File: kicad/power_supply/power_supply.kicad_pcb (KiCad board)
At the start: 2 copper layers, 36.6 x 24.1 mm, 18 parts, among them J1 USB_C_Receptacle_PowerOnly_6P, J2 Battery terminal, J3 Base board terminal, Q1 DMG2301L, U1 MCP1640x-xCHY, U2 MCP73831-2-OT

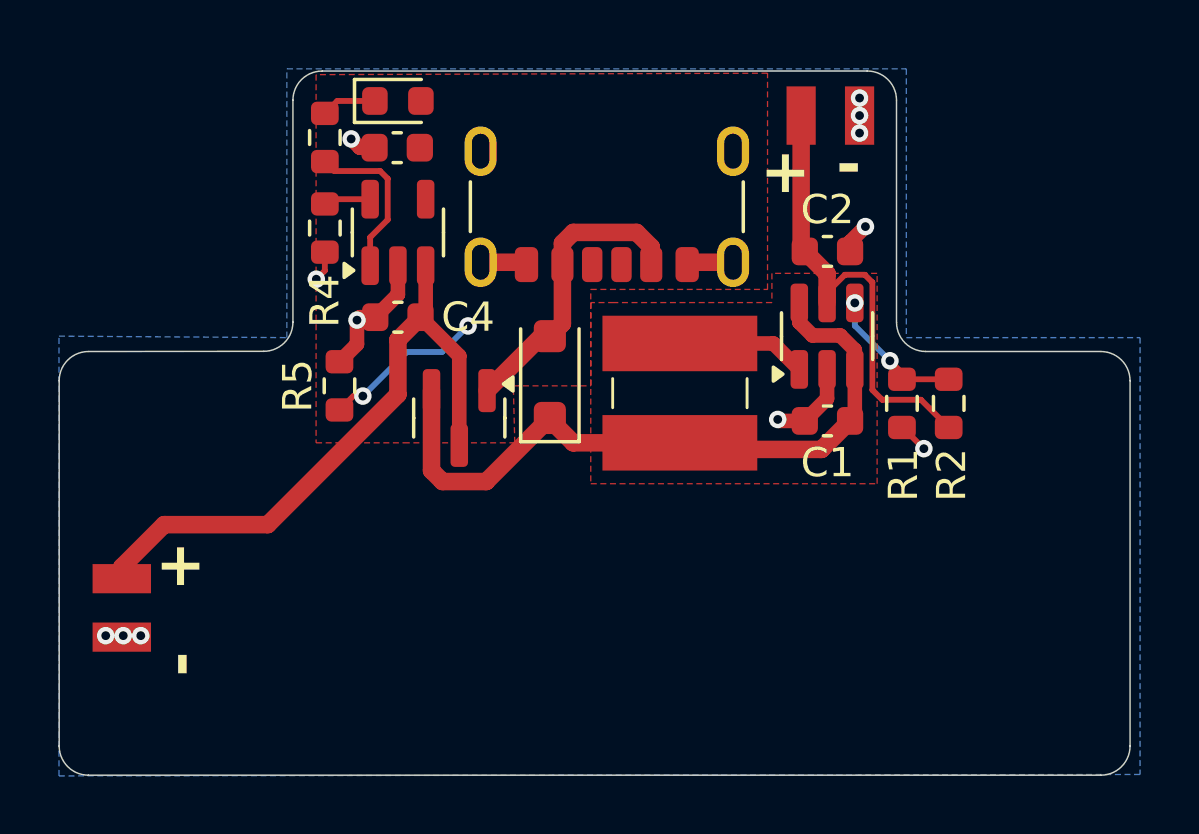
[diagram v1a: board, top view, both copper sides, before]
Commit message: pcbs: improve powering scheme, redesign cartridge; 3dcad: update whole housing
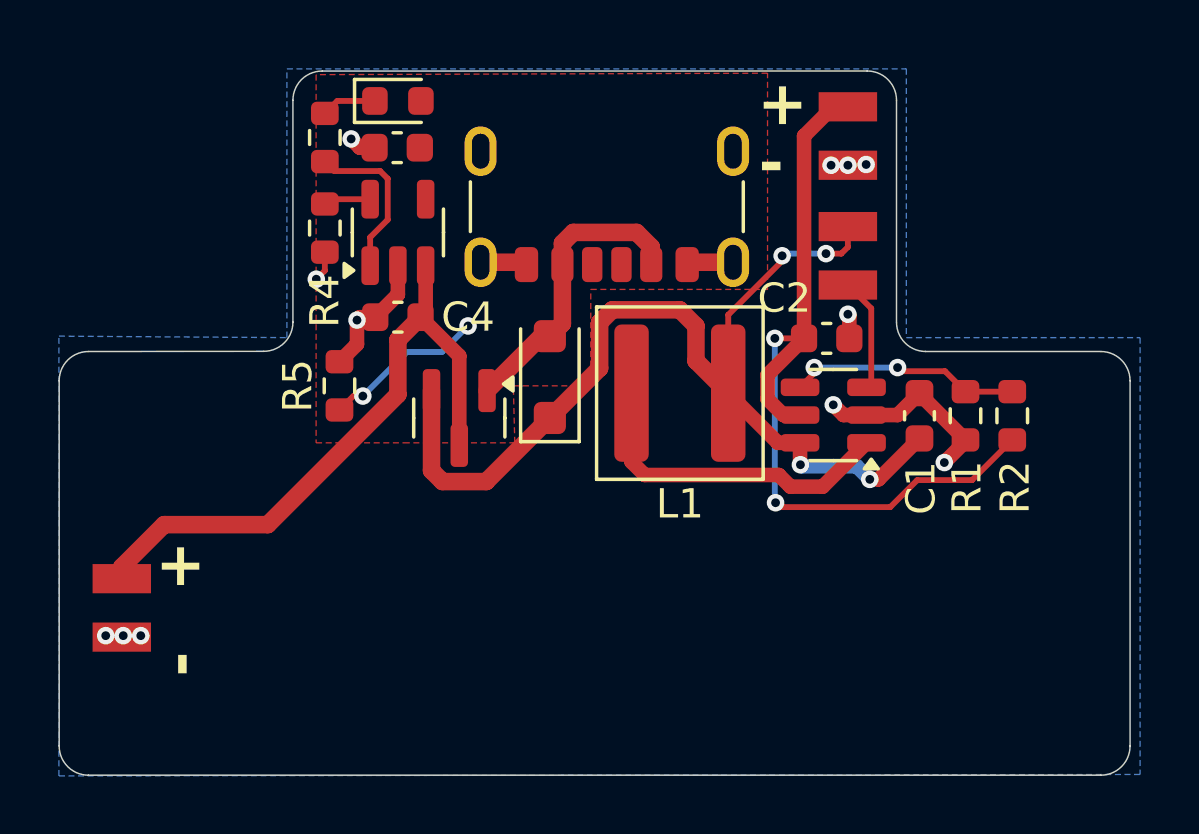
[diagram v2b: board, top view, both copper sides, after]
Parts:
- added J4: Short if cartridge present, components:Pads_1x2mm_2x, F.Cu at (152.0, 82.2)
- J3: value Base board terminal -> Base board power terminal
- L1: footprint components:CDRH4D18 -> Inductor_SMD:L_Coilcraft_XAL5050-XXX
- moved C1 3.15 mm to (154.4, 87.7), turned to 90 degrees
- moved C2 2.98 mm to (151.3, 85.0)
- moved U1 2.71 mm to (151.5, 87.7), turned to 180 degrees
- moved R1 2.22 mm to (156.0, 87.7)
- moved R2 2.22 mm to (157.6, 87.7)
- moved J3 0.92 mm to (152.0, 78.1), turned to -90 degrees
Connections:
- U1 pad 3: VSYS -> Net-(J4-Pin_1)
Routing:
- net Net-(J3-Pin_1): track 16.3 -> 28.5 mm, vias 0 -> 2
- net VSYS: track 24.4 -> 35.7 mm, vias 0 -> 4
- net Net-(U1-SW): track 4.46 -> 11.4 mm
- net Net-(J4-Pin_1): track 0.00 -> 3.90 mm
- net Net-(U1-V_{FB}): track 4.88 -> 7.99 mm
- net GND: track 14.7 -> 17.2 mm
- removed copper zone on F.Cu, net VSYS

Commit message: 3dcad/housing: fdm & sla variants; kicad/power_supply: add p-down resistor to the MCP1640's EN pin
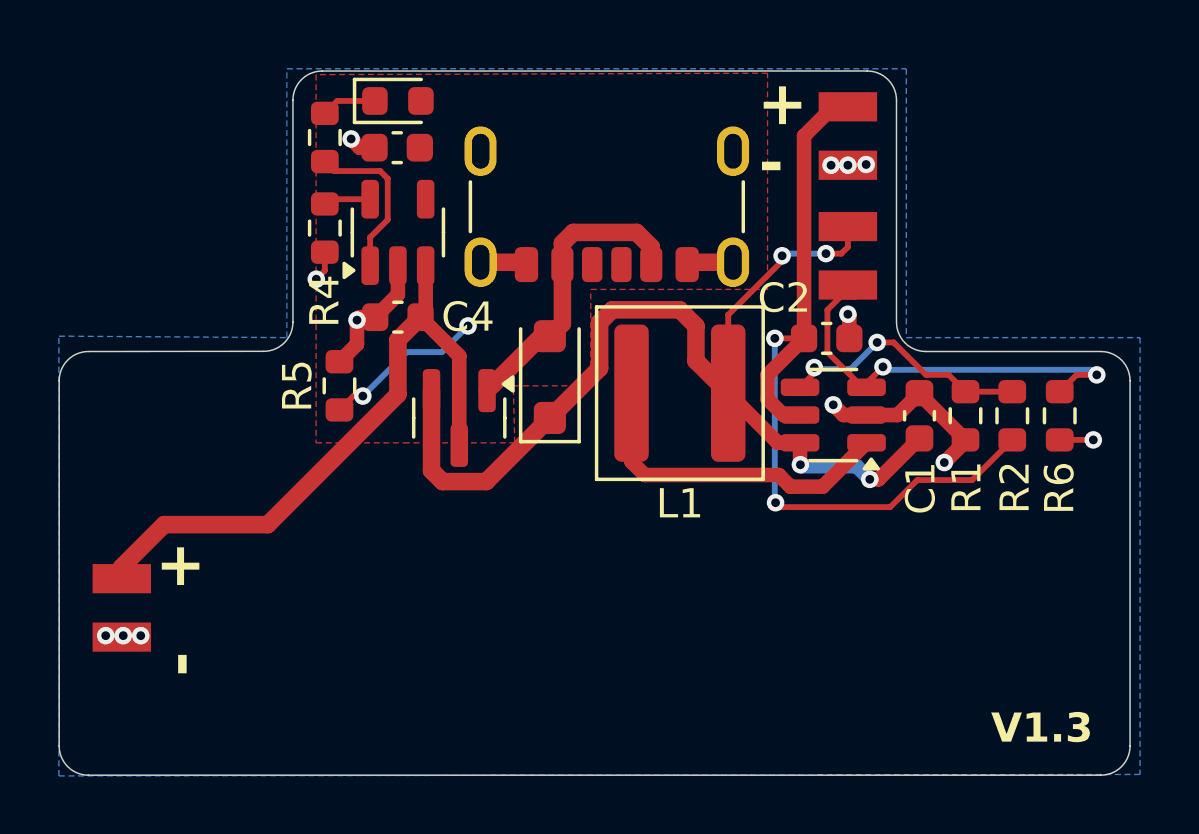
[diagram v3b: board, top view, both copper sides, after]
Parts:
- added R6: 309K, Resistor_SMD:R_0603_1608Metric, F.Cu at (159.2, 87.7)
- J4: value Short if cartridge present -> Shorted if cartridge present
- R3: value 470R -> 200R
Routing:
- net Net-(J4-Pin_1): track 3.90 -> 14.8 mm, vias 0 -> 2
- net GND: track 17.2 -> 18.3 mm, vias 12 -> 13
- net Net-(U1-V_{FB}): track 7.99 -> 8.75 mm
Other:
- board text added: "V1.3"
